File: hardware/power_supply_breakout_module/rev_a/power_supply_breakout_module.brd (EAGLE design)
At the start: 68.1 x 66 mm, 26 parts, among them J1 MODULE_POWER, J2 SCREW-TERMINAL_2_0.100, J3 SCREW-TERMINAL_2_0.100, J4 SCREW-TERMINAL_7_0.100, J5 SCREW-TERMINAL_2_0.100

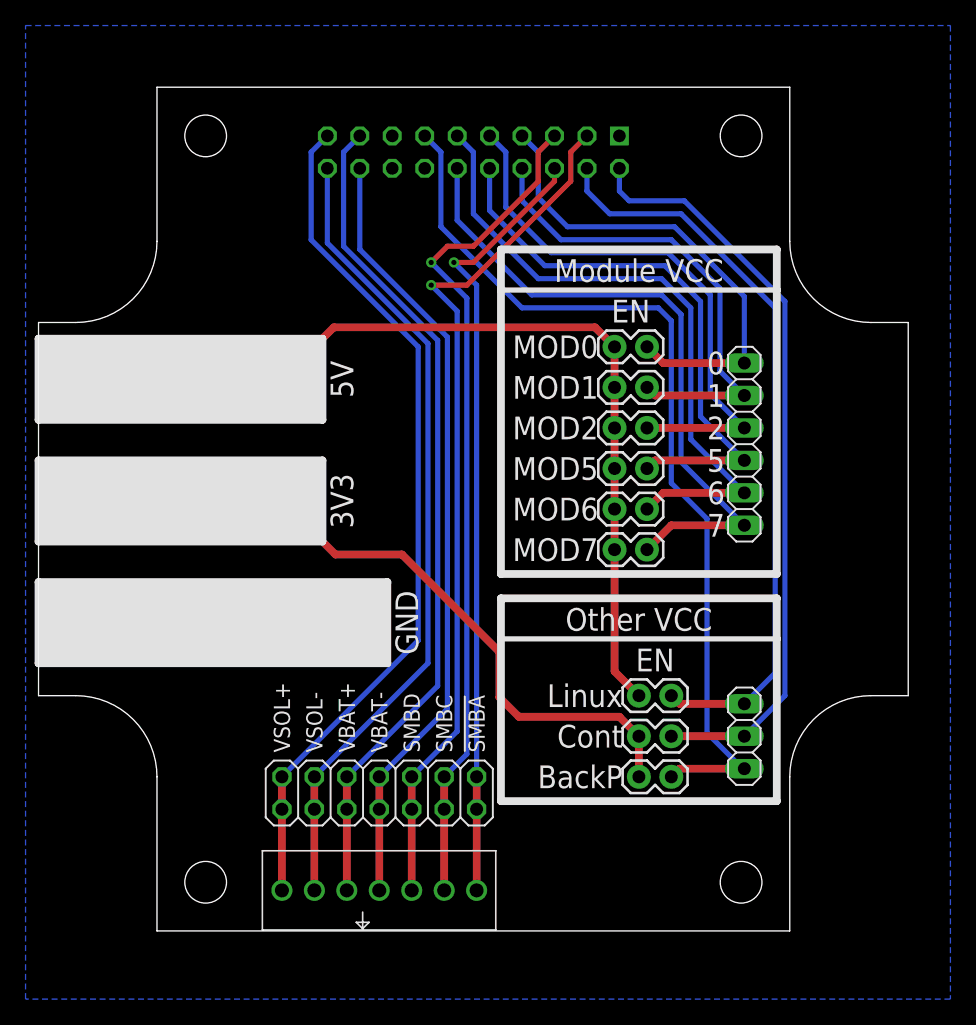
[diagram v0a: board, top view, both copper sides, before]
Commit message: doc on power supply breakout
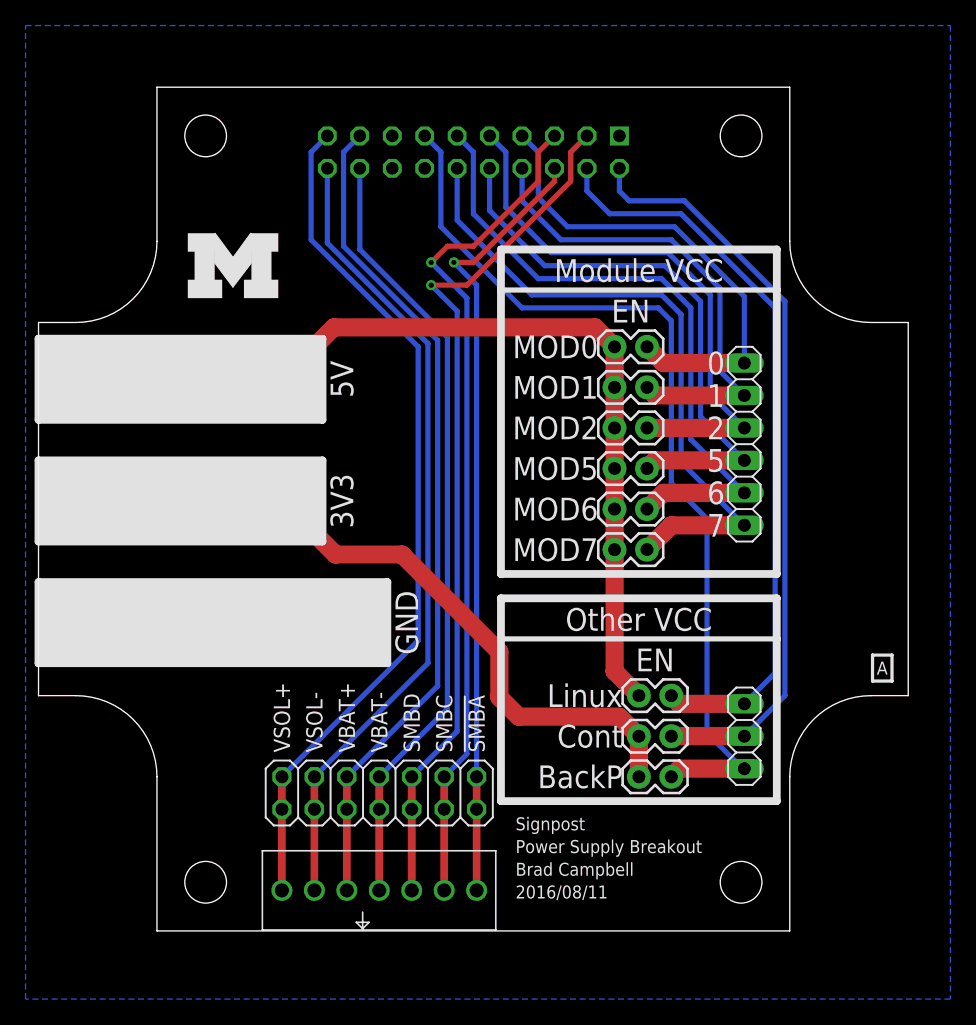
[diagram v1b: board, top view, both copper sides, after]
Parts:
- added LOGO1: UMICH_SOLID_MEDIUM, logos:UMICH_SOLID_200MIL
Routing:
- net GND: track 58.2 -> 0.00 mm
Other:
- board text added: "2016/08/11"
- board text added: "A"
- board text added: "Brad Campbell"
- board text added: "Power Supply Breakout"
- board text added: "Signpost"
